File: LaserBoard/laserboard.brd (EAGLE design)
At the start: 76.2 x 76.2 mm, 22 parts, among them J1 PJ-002AH-SMT-TR, Q1 BSS138, X1 22-23-2021, X2 22-23-2021

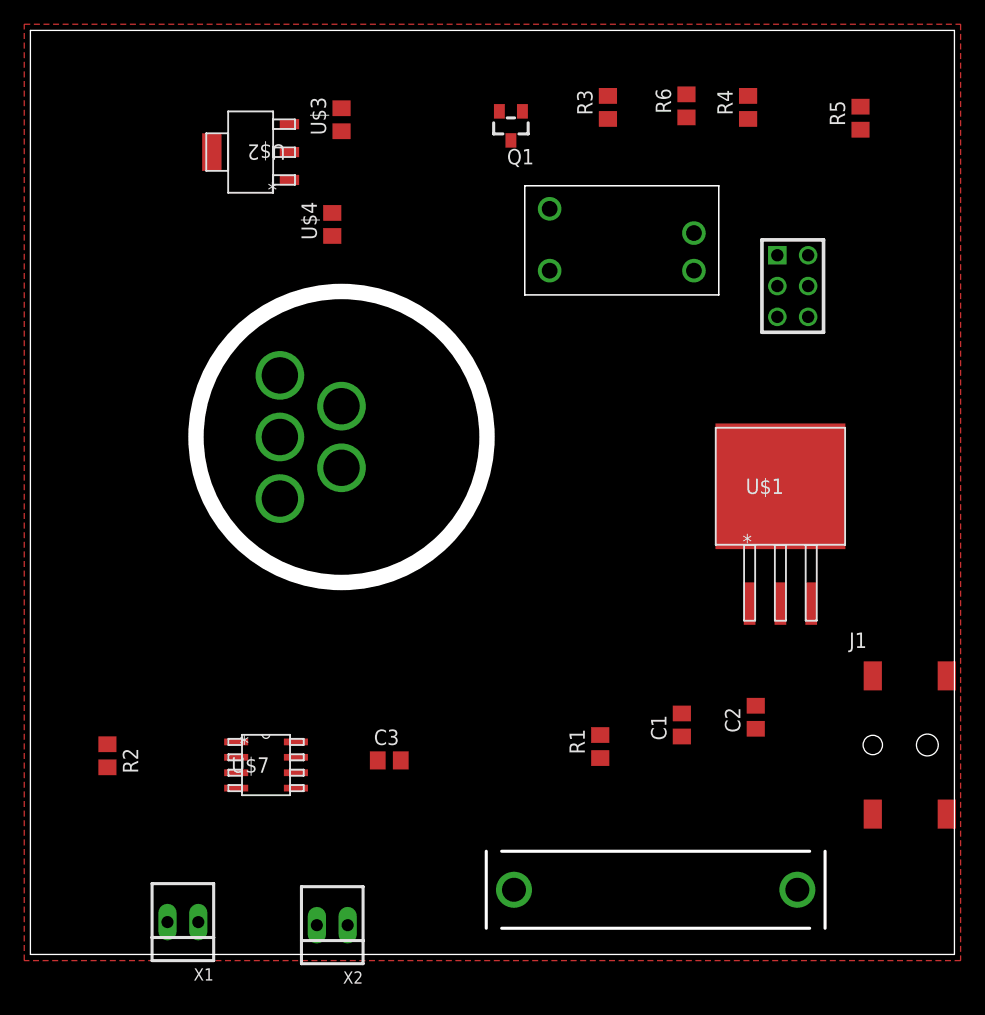
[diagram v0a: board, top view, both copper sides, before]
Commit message: Utilized Christian's Updated Library
Reloaded ChristiansCustom library to make use of the updated components
submitted by Christian.
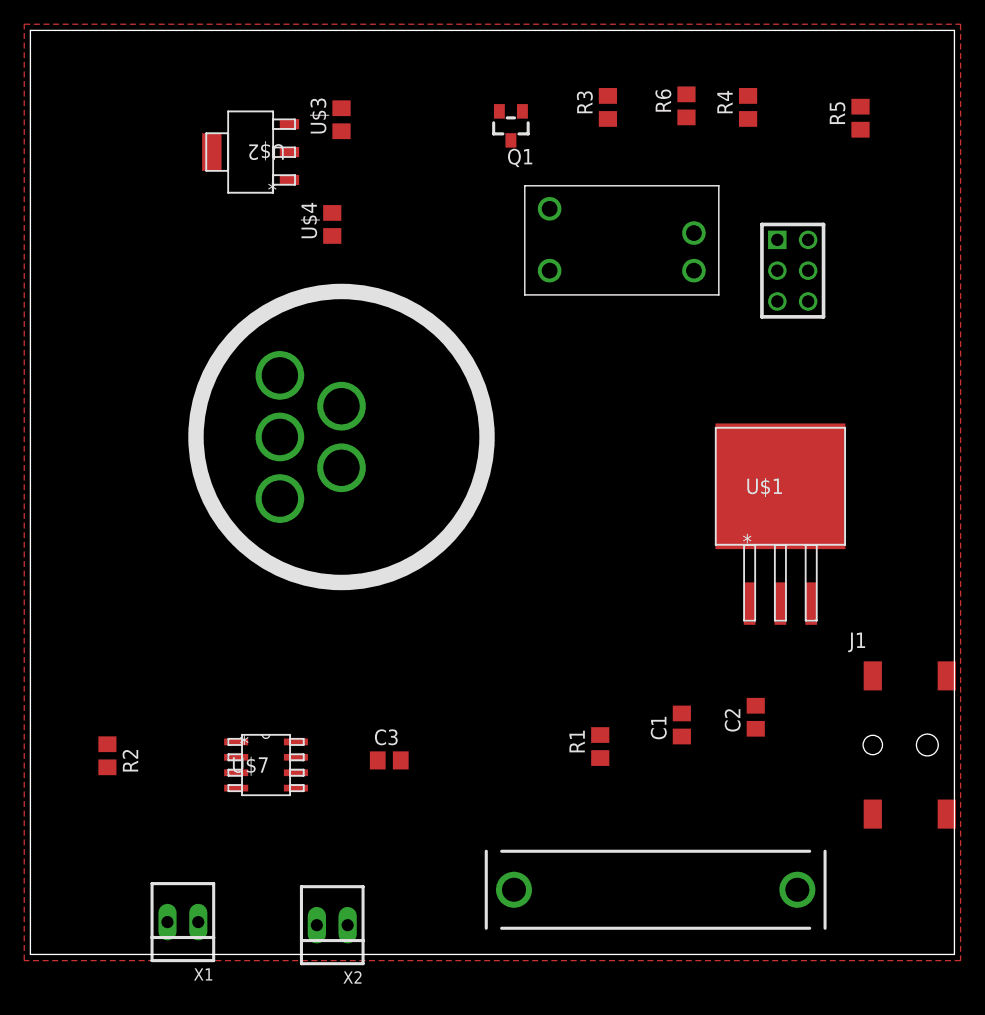
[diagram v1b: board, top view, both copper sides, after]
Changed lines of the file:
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@@
 <vertex x="-0.508" y="-0.508"/>
 </polygon>
-<wire x1="54.718" y1="56.388" x2="61.595" y2="57.658" width="0" layer="19" extent="1-1"/>
-<wire x1="25.654" y1="40.132" x2="24.892" y2="61.148" width="0" layer="19" extent="1-1"/>
 </signal>
 <signal name="+3V3">
@@
 <contactref element="Q1" pad="1"/>
 <contactref element="R3" pad="2"/>
-<wire x1="47.625" y1="70.8" x2="61.595" y2="55.118" width="0" layer="19" extent="1-1"/>
+<wire x1="47.625" y1="70.8" x2="61.595" y2="56.388" width="0" layer="19" extent="1-1"/>
 <wire x1="40.574" y1="69.526" x2="47.625" y2="70.8" width="0" layer="19" extent="1-1"/>
 <wire x1="24.892" y1="59.248" x2="40.574" y2="69.526" width="0" layer="19" extent="1-1"/>
@@
 <contactref element="R1" pad="2"/>
 <contactref element="U$8" pad="2"/>
-<wire x1="59.309" y1="28.9306" x2="64.135" y2="57.658" width="0" layer="19" extent="1-1"/>
+<wire x1="59.309" y1="28.9306" x2="64.135" y2="58.928" width="0" layer="19" extent="1-1"/>
 <wire x1="53.721" y1="17.973" x2="59.309" y2="28.9306" width="0" layer="19" extent="1-1"/>
 <wire x1="46.99" y1="18.095" x2="53.721" y2="17.973" width="0" layer="19" extent="1-1"/>
@@
 <contactref element="R2" pad="1"/>
 <contactref element="U$8" pad="4"/>
-<wire x1="16.9672" y1="13.716" x2="64.135" y2="55.118" width="0" layer="19" extent="1-1"/>
+<wire x1="16.9672" y1="13.716" x2="64.135" y2="56.388" width="0" layer="19" extent="1-1"/>
 <wire x1="6.35" y1="17.333" x2="16.9672" y2="13.716" width="0" layer="19" extent="1-1"/>
 </signal>
@@
 <contactref element="R3" pad="1"/>
 <contactref element="Q1" pad="2"/>
+<wire x1="47.625" y1="68.9" x2="61.595" y2="53.848" width="0" layer="19" extent="1-1"/>
 <wire x1="38.674" y1="69.526" x2="47.625" y2="68.9" width="0" layer="19" extent="1-1"/>
-<wire x1="61.595" y1="52.578" x2="47.625" y2="68.9" width="0" layer="19" extent="1-1"/>
 </signal>
 <signal name="N$5">

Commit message: Completed Layout of the Laser PCB
This is the completed layout of the Laser PCB. All components and traces
have been laid. The final DRC before manufacturing has not been
performed.
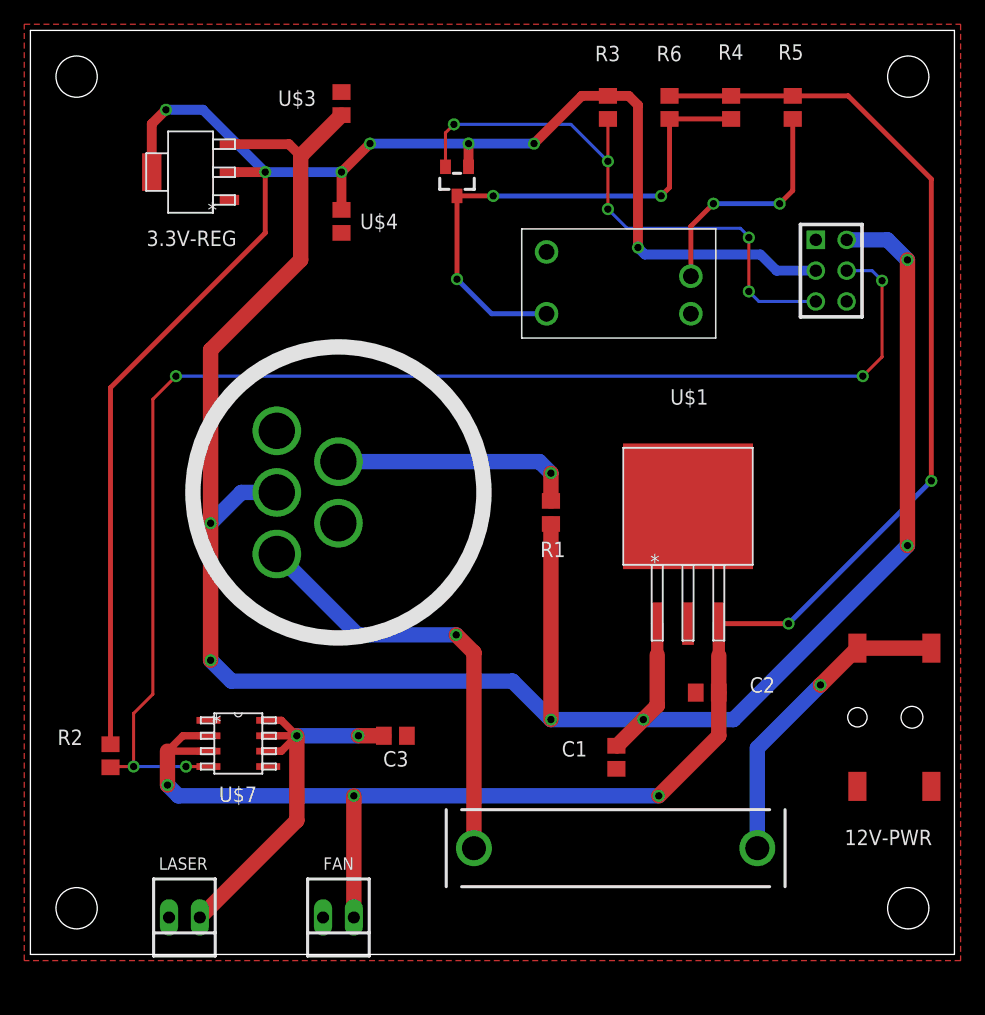
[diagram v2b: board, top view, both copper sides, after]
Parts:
- removed J1: PJ-002AH-SMT-TR, PJ-002AH-SMT-TR:CUI_PJ-002AH-SMT-TR
- removed U$2: LMS8117AMP-3.3/NOPB, LMS8117AMP-3_3NOPB:MP04A
- removed X1, X2: 22-23-2021, con-molex:22-23-2021
- added 12V-PWR: PJ-002AH-SMT-TR, PJ-002AH-SMT-TR:CUI_PJ-002AH-SMT-TR
- added 3.3V-REG: LMS8117AMP-3.3/NOPB, LMS8117AMP-3_3NOPB:MP04A
- added FAN, LASER: 22-23-2021, con-molex:22-23-2021
- U$3: value 10uF Tantalum -> 10uF Tant.
- U$4: value 10UF Tantalum -> 10uF Tant.
- moved R1 19.7 mm to (42.9, 36.4), turned to 270 degrees
- moved U$1 7.80 mm to (54.2, 37.0)
- moved Q1 6.38 mm to (35.2, 63.8)
- moved C1 6.02 mm to (48.3, 16.3), turned to 270 degrees
- moved R5 5.66 mm to (62.9, 69.8), turned to 270 degrees
- moved U$6 4.76 mm to (48.3, 8.76), turned to 180 degrees
- moved U$5 4.58 mm to (25.4, 38.1)
- moved C2 4.49 mm to (55.8, 21.6), turned to 180 degrees
- moved U$9 3.57 mm to (48.5, 52.8)
- moved U$8 3.18 mm to (66.0, 56.4)
- moved U$7 2.90 mm to (17.1, 17.4)
- moved C3 2.09 mm to (30.1, 18.0)
- moved R6 1.40 mm to (52.7, 69.8), turned to 270 degrees
- moved R4 1.40 mm to (57.8, 69.8)
- moved U$3 1.33 mm to (25.7, 70.2)
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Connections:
- net +12V: now also 3.3V-REG.3; no longer U$2.3
- net +3V3: now also 3.3V-REG.2, 3.3V-REG.4; no longer U$2.2, U$2.4
- net +5V: now also FAN.1; no longer X2.1
- net GND: now also 12V-PWR.2, 12V-PWR.3, 3.3V-REG.1, FAN.2, LASER.2; no longer J1.2, J1.3, U$2.1, X1.2, X2.2
- net LSR_PWR: now also LASER.1; no longer X1.1
- net N$2: now also 12V-PWR.1.1, 12V-PWR.1.2; no longer J1.1.1, J1.1.2
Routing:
- net +12V: track 0.00 -> 184.6 mm, vias 0 -> 6
- net +5V: track 0.00 -> 149.0 mm, vias 0 -> 5
- net +3V3: track 0.00 -> 137.3 mm, vias 0 -> 7
- net LSR_EN: track 0.00 -> 110.2 mm, vias 0 -> 5
- net TILT: track 0.00 -> 48.1 mm, vias 0 -> 5
- net N$5: track 0.00 -> 44.0 mm, vias 0 -> 3
- net N$3: track 0.00 -> 35.8 mm, vias 0 -> 1
- net LSR_PWR: track 0.00 -> 33.6 mm, vias 0 -> 2
- net N$2: track 0.00 -> 26.0 mm, vias 0 -> 1
- net N$1: track 0.00 -> 20.2 mm, vias 0 -> 1
- net N$7: track 0.00 -> 19.6 mm, vias 0 -> 2
